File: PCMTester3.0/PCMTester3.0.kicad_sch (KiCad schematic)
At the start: 63 parts

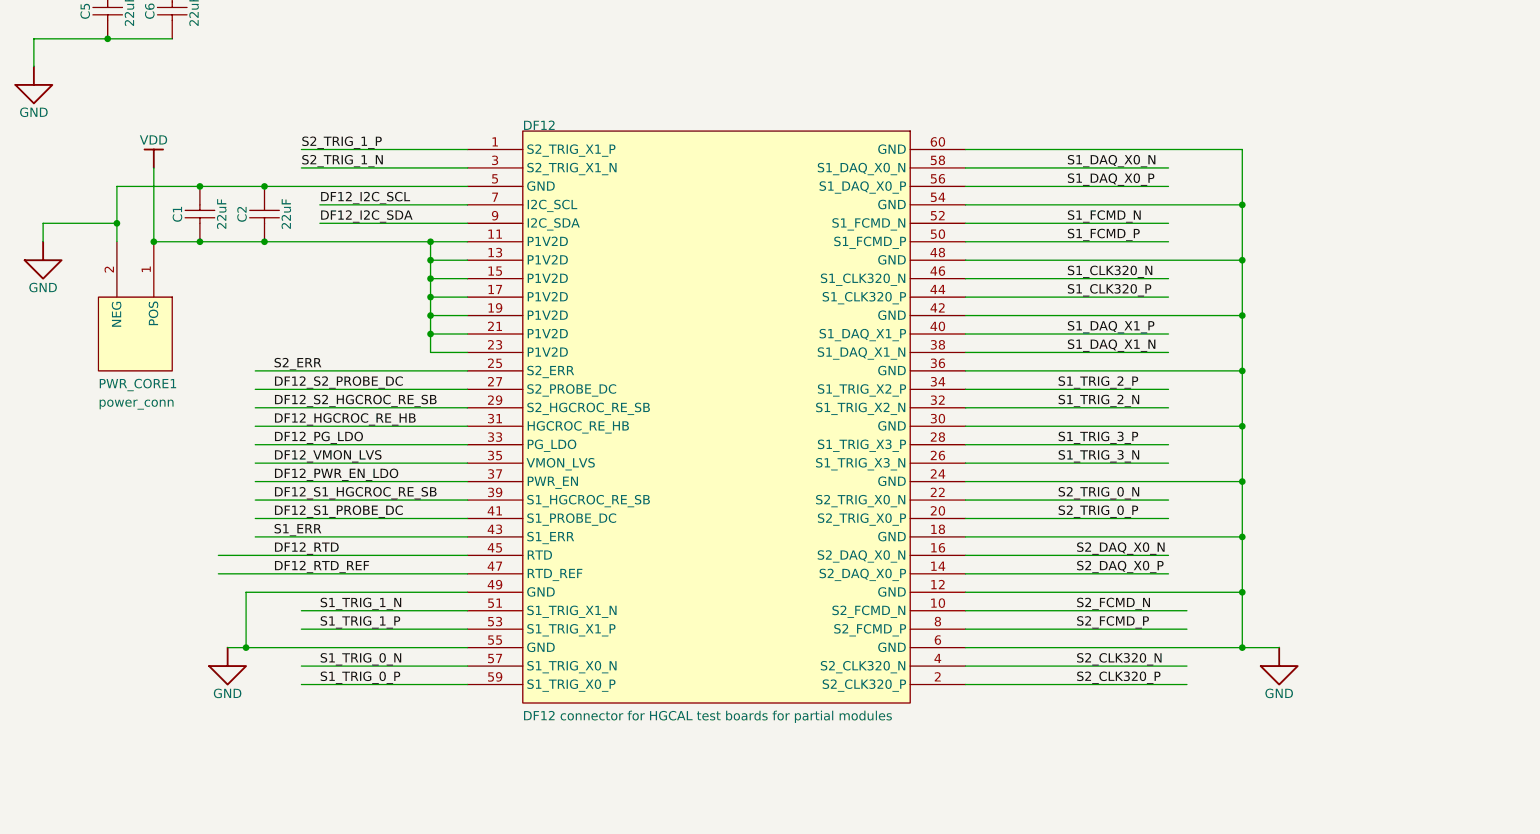
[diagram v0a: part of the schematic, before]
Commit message: adding schematic with updated DF12 pins
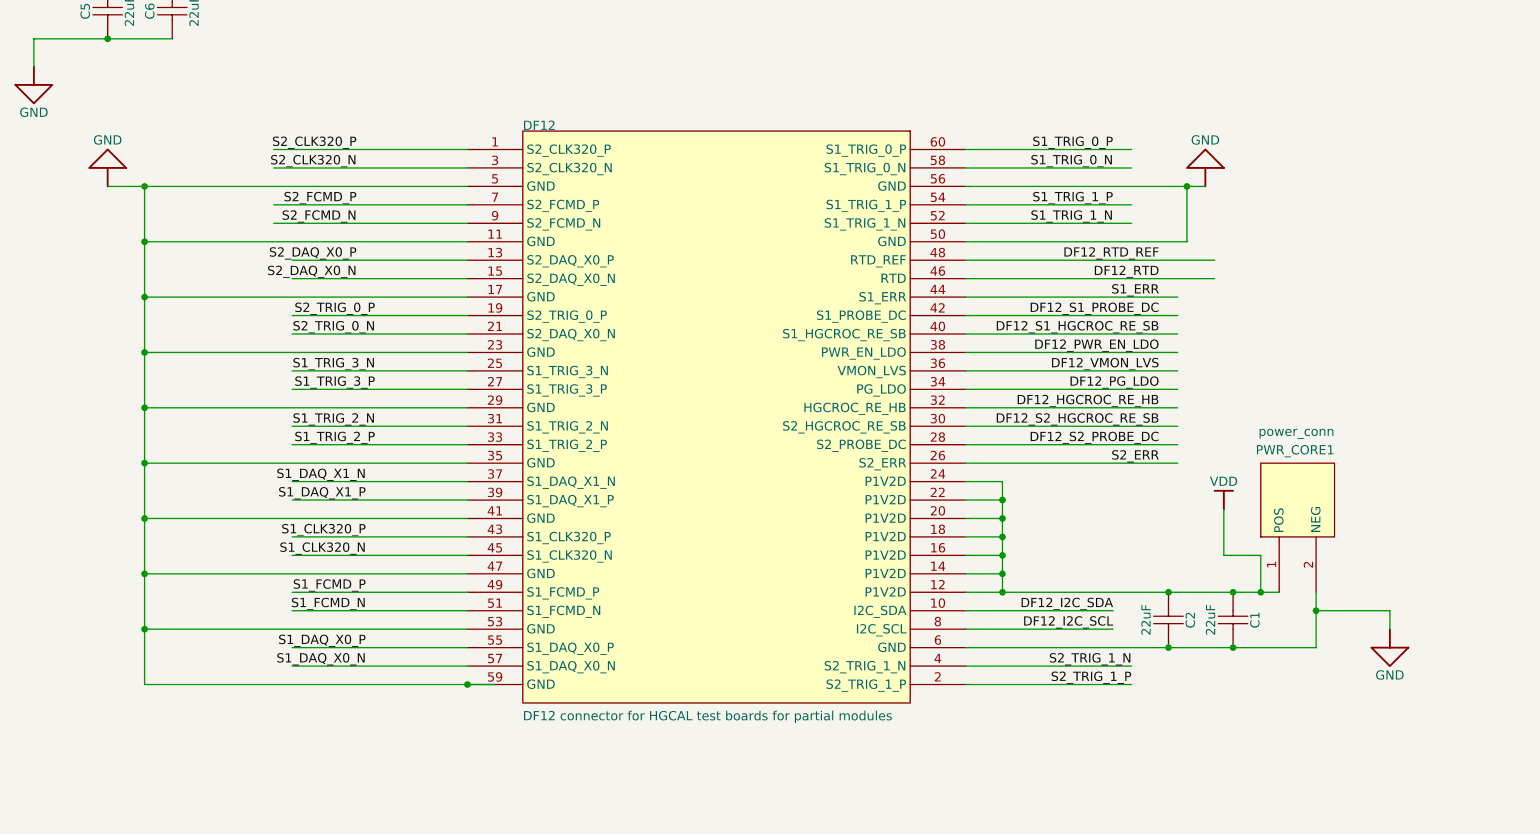
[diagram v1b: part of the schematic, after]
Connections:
- net DF12_HGCROC_RE_HB: now also DF12.32 (HGCROC_RE_HB); no longer DF12.31 (HGCROC_RE_HB)
- net DF12_I2C_SCL: now also DF12.8 (I2C_SCL); no longer DF12.7 (I2C_SCL)
- net DF12_I2C_SDA: now also DF12.10 (I2C_SDA); no longer DF12.9 (I2C_SDA)
- net DF12_PG_LDO: now also DF12.34 (PG_LDO); no longer DF12.33 (PG_LDO)
- net DF12_PWR_EN_LDO: now also DF12.38 (PWR_EN_LDO); no longer DF12.37 (PWR_EN)
- net DF12_RTD: now also DF12.46 (RTD); no longer DF12.45 (RTD)
- net DF12_RTD_REF: now also DF12.48 (RTD_REF); no longer DF12.47 (RTD_REF)
- net DF12_S1_HGCROC_RE_SB: now also DF12.40 (S1_HGCROC_RE_SB); no longer DF12.39 (S1_HGCROC_RE_SB)
- net DF12_S1_PROBE_DC: now also DF12.42 (S1_PROBE_DC); no longer DF12.41 (S1_PROBE_DC)
- net DF12_S2_HGCROC_RE_SB: now also DF12.30 (S2_HGCROC_RE_SB); no longer DF12.29 (S2_HGCROC_RE_SB)
- net DF12_S2_PROBE_DC: now also DF12.28 (S2_PROBE_DC); no longer DF12.27 (S2_PROBE_DC)
- net DF12_VMON_LVS: now also DF12.36 (VMON_LVS); no longer DF12.35 (VMON_LVS)
- net GND: now also DF12.11 (GND), DF12.17 (GND), DF12.23 (GND), DF12.29 (GND), DF12.35 (GND), DF12.41 (GND), DF12.47 (GND), DF12.50 (GND), DF12.53 (GND), DF12.56 (GND), DF12.59 (GND); no longer DF12.12 (GND), DF12.18 (GND), DF12.24 (GND), DF12.30 (GND), DF12.36 (GND), DF12.42 (GND), DF12.48 (GND), DF12.49 (GND), DF12.54 (GND), DF12.55 (GND), DF12.60 (GND)
- net S1_CLK320_N: now also DF12.45 (S1_CLK320_N); no longer DF12.46 (S1_CLK320_N)
- net S1_CLK320_P: now also DF12.43 (S1_CLK320_P); no longer DF12.44 (S1_CLK320_P)
- net S1_DAQ_X0_N: now also DF12.57 (S1_DAQ_X0_N); no longer DF12.58 (S1_DAQ_X0_N)
- net S1_DAQ_X0_P: now also DF12.55 (S1_DAQ_X0_P); no longer DF12.56 (S1_DAQ_X0_P)
- net S1_DAQ_X1_N: now also DF12.37 (S1_DAQ_X1_N); no longer DF12.38 (S1_DAQ_X1_N)
- net S1_DAQ_X1_P: now also DF12.39 (S1_DAQ_X1_P); no longer DF12.40 (S1_DAQ_X1_P)
- net S1_ERR: now also DF12.44 (S1_ERR); no longer DF12.43 (S1_ERR)
- net S1_FCMD_N: now also DF12.51 (S1_FCMD_N); no longer DF12.52 (S1_FCMD_N)
- net S1_FCMD_P: now also DF12.49 (S1_FCMD_P); no longer DF12.50 (S1_FCMD_P)
- net S1_TRIG_0_N: now also DF12.58 (S1_TRIG_0_N); no longer DF12.57 (S1_TRIG_X0_N)
- net S1_TRIG_0_P: now also DF12.60 (S1_TRIG_0_P); no longer DF12.59 (S1_TRIG_X0_P)
- net S1_TRIG_1_N: now also DF12.52 (S1_TRIG_1_N); no longer DF12.51 (S1_TRIG_X1_N)
- net S1_TRIG_1_P: now also DF12.54 (S1_TRIG_1_P); no longer DF12.53 (S1_TRIG_X1_P)
- net S1_TRIG_2_N: now also DF12.31 (S1_TRIG_2_N); no longer DF12.32 (S1_TRIG_X2_N)
- net S1_TRIG_2_P: now also DF12.33 (S1_TRIG_2_P); no longer DF12.34 (S1_TRIG_X2_P)
- net S1_TRIG_3_N: now also DF12.25 (S1_TRIG_3_N); no longer DF12.26 (S1_TRIG_X3_N)
- net S1_TRIG_3_P: now also DF12.27 (S1_TRIG_3_P); no longer DF12.28 (S1_TRIG_X3_P)
- net S2_CLK320_N: now also DF12.3 (S2_CLK320_N); no longer DF12.4 (S2_CLK320_N)
- net S2_CLK320_P: now also DF12.1 (S2_CLK320_P); no longer DF12.2 (S2_CLK320_P)
- net S2_DAQ_X0_N: now also DF12.15 (S2_DAQ_X0_N); no longer DF12.16 (S2_DAQ_X0_N)
- net S2_DAQ_X0_P: now also DF12.13 (S2_DAQ_X0_P); no longer DF12.14 (S2_DAQ_X0_P)
- net S2_ERR: now also DF12.26 (S2_ERR); no longer DF12.25 (S2_ERR)
- net S2_FCMD_N: now also DF12.9 (S2_FCMD_N); no longer DF12.10 (S2_FCMD_N)
- net S2_FCMD_P: now also DF12.7 (S2_FCMD_P); no longer DF12.8 (S2_FCMD_P)
- net S2_TRIG_0_N: now also DF12.21 (S2_DAQ_X0_N); no longer DF12.22 (S2_TRIG_X0_N)
- net S2_TRIG_0_P: now also DF12.19 (S2_TRIG_0_P); no longer DF12.20 (S2_TRIG_X0_P)
- net S2_TRIG_1_N: now also DF12.4 (S2_TRIG_1_N); no longer DF12.3 (S2_TRIG_X1_N)
- net S2_TRIG_1_P: now also DF12.2 (S2_TRIG_1_P); no longer DF12.1 (S2_TRIG_X1_P)
- net VDD: now also DF12.12 (P1V2D), DF12.14 (P1V2D), DF12.16 (P1V2D), DF12.18 (P1V2D), DF12.20 (P1V2D), DF12.22 (P1V2D), DF12.24 (P1V2D); no longer DF12.11 (P1V2D), DF12.13 (P1V2D), DF12.15 (P1V2D), DF12.17 (P1V2D), DF12.19 (P1V2D), DF12.21 (P1V2D), DF12.23 (P1V2D)
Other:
- moved on the sheet: C1, C2, PWR_CORE1
